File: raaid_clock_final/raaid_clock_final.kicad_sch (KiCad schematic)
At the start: 55 parts, among them J1 Conn_01x06, J2 Power_inlet_vertical, J3 Conn_02x03_Odd_Even, Q1 NPN_2N3904_SOT23, SW1 Omron_B3F_SPST, SW2 Omron_B3F_SPST, SW3 Omron_B3F_SPST, SW4 Omron_B3F_SPST, SW5 Omron_B3F_SPST, U1 ATmega328-PU, U2 L7805, U3 MAX7219, U4 UltrasonicModule, U5 DS1307_DIP-8, Y1 Crystal_16MHz, Y2 Crystal_32768Hz

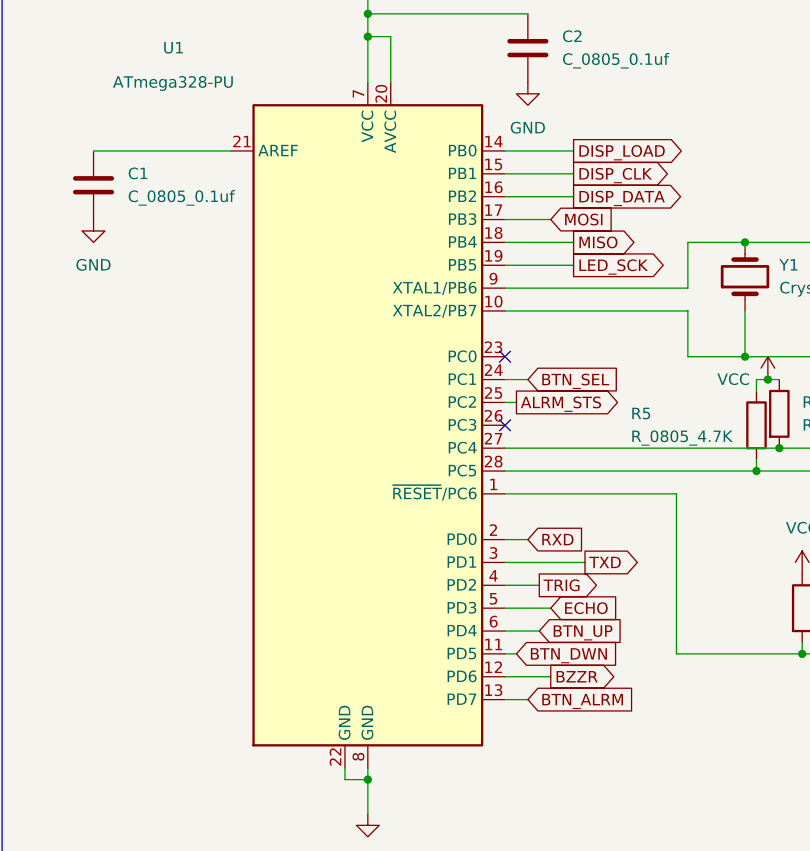
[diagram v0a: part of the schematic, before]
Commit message: moved inlet; redid gerbers
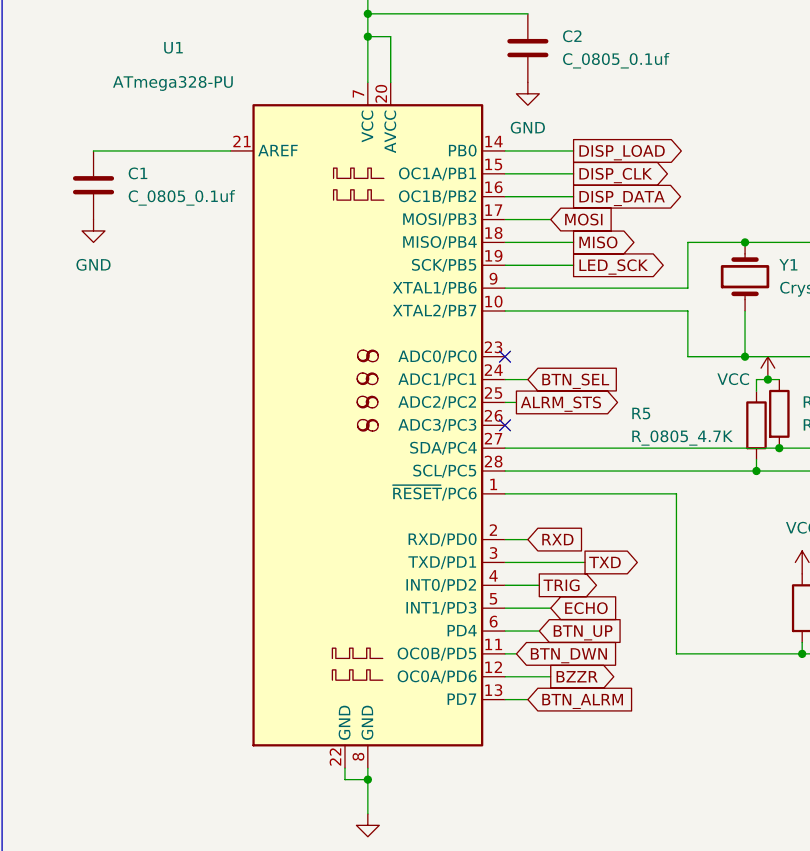
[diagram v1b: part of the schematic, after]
